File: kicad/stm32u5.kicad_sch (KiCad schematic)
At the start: 10 parts, among them SW5 BOOTSEL, U12 STM32U535CET6-modified

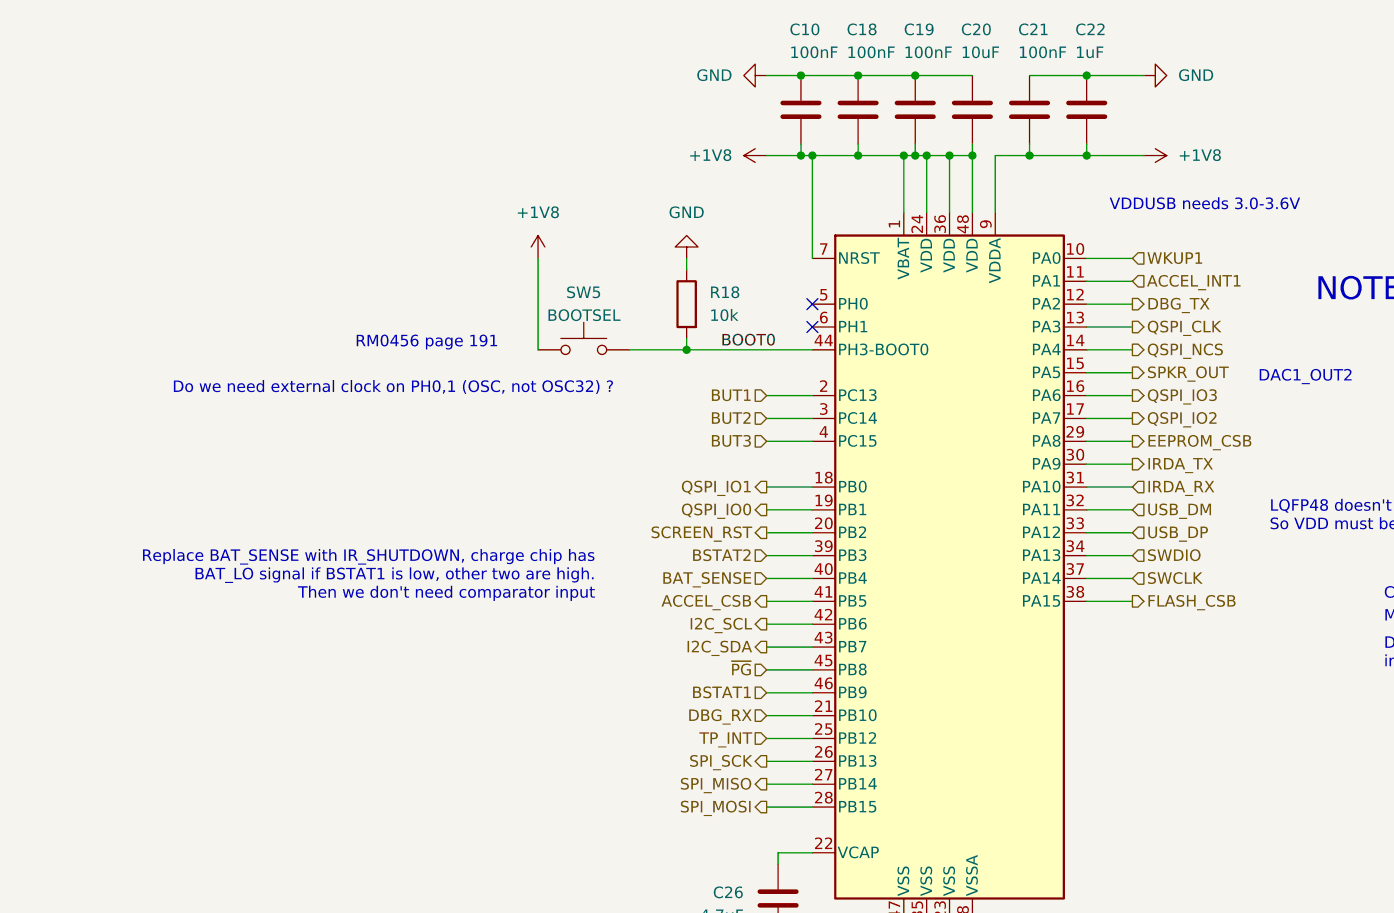
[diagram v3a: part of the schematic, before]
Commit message: hw: change to 3v3 LDO and remove unnecessary MCU pins
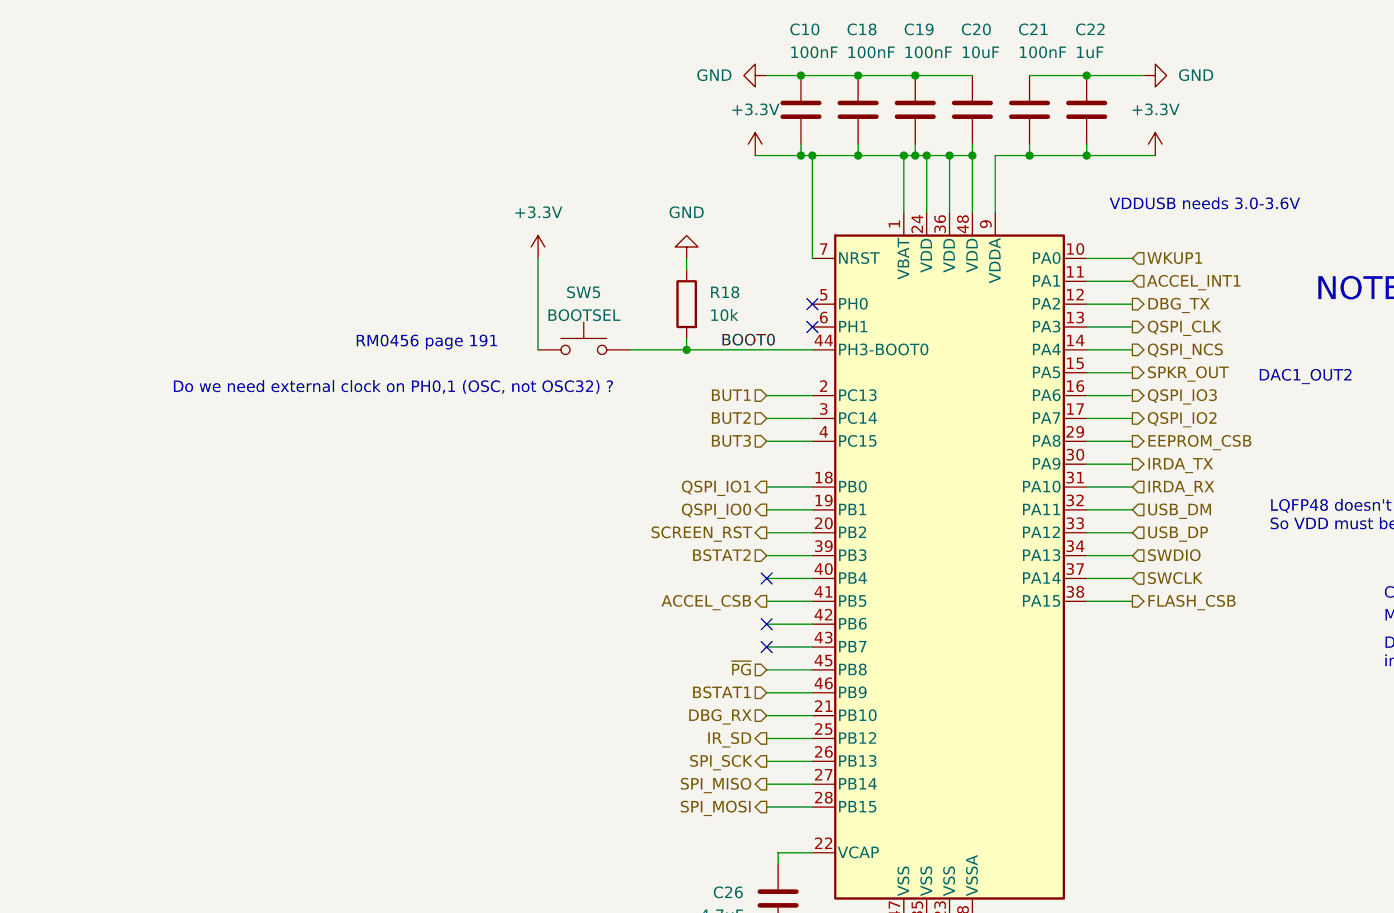
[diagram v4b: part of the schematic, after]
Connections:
- net +1V8 renamed +3.3V
- net BAT_SENSE: no longer names the net of U12.40 (PB4)
- net I2C_SCL: no longer names the net of U12.42 (PB6)
- net I2C_SDA: no longer names the net of U12.43 (PB7)
- net TP_INT renamed IR_SD
- no-connect marks 2 -> 5
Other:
- note removed: "Replace BAT_SENSE with IR_SHUTDOWN, charge chip has BAT_LO signal if BSTAT1 is low, other two are high. Then we don't need comparator input"
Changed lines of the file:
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@@
   (junction (at 110.49 33.02) (diameter 0) (color 0 0 0 0)
   )
+  (no_connect (at 95.25 85.09))
   (no_connect (at 100.33 52.07))
+  (no_connect (at 95.25 80.01))
+  (no_connect (at 95.25 87.63))
   (no_connect (at 100.33 49.53))
   (wire (pts (xy 115.57 33.02) (xy 118.11 33.02))
@@
     (stroke (width 0) (type default))
   )
+  (wire (pts (xy 130.81 33.02) (xy 138.43 33.02))
+    (stroke (width 0) (type default))
+  )
   (wire (pts (xy 130.81 64.77) (xy 135.89 64.77))
     (stroke (width 0) (type default))
@@
     (stroke (width 0) (type default))
   )
-  (wire (pts (xy 95.25 33.02) (xy 99.06 33.02))
+  (wire (pts (xy 93.98 33.02) (xy 99.06 33.02))
     (stroke (width 0) (type default))
   )
@@
     (stroke (width 0) (type default))
   )
+  (wire (pts (xy 95.25 97.79) (xy 100.33 97.79))
+    (stroke (width 0) (type default))
+  )
   (wire (pts (xy 130.81 82.55) (xy 135.89 82.55))
     (stroke (width 0) (type default))
@@
     (stroke (width 0) (type default))
   )
-  (wire (pts (xy 130.81 33.02) (xy 137.16 33.02))
-    (stroke (width 0) (type default))
-  )
   (wire (pts (xy 100.33 110.49) (xy 96.52 110.49))
     (stroke (width 0) (type default))
@@
   )
   (wire (pts (xy 110.49 119.38) (xy 96.52 119.38))
-    (stroke (width 0) (type default))
-  )
-  (wire (pts (xy 95.25 97.79) (xy 100.33 97.79))
     (stroke (width 0) (type default))
   )
@@
     (effects (font (size 1.27 1.27)) (justify left bottom))
   )
-  (text "Replace BAT_SENSE with IR_SHUTDOWN, charge chip has \nBAT_LO signal if BSTAT1 is low, other two are high.\nThen we don't need comparator input"
-    (at 76.2 82.55 0)
-    (effects (font (size 1.27 1.27)) (justify right bottom))
-  )
   (text "DAC1_OUT2" (at 149.86 58.42 0)
     (effects (font (size 1.27 1.27)) (justify left bottom))
@@
     (effects (font (size 1.27 1.27)) (justify right))
   )
-  (hierarchical_label "I2C_SDA" (shape output) (at 95.25 87.63 180) (fields_autoplaced)
-    (effects (font (size 1.27 1.27)) (justify right))
-  )
   (hierarchical_label "QSPI_IO0" (shape output) (at 95.25 72.39 180) (fields_autoplaced)
     (effects (font (size 1.27 1.27)) (justify right))
@@
     (effects (font (size 1.27 1.27)) (justify right))
   )
-  (hierarchical_label "TP_INT" (shape input) (at 95.25 97.79 180) (fields_autoplaced)
-    (effects (font (size 1.27 1.27)) (justify right))
-  )
   (hierarchical_label "BUT3" (shape input) (at 95.25 64.77 180) (fields_autoplaced)
     (effects (font (size 1.27 1.27)) (justify right))
@@
     (effects (font (size 1.27 1.27)) (justify left))
   )
-  (hierarchical_label "I2C_SCL" (shape output) (at 95.25 85.09 180) (fields_autoplaced)
-    (effects (font (size 1.27 1.27)) (justify right))
-  )
   (hierarchical_label "BSTAT2" (shape input) (at 95.25 77.47 180) (fields_autoplaced)
     (effects (font (size 1.27 1.27)) (justify right))
@@
     (effects (font (size 1.27 1.27)) (justify left))
   )
-  (hierarchical_label "BAT_SENSE" (shape input) (at 95.25 80.01 180) (fields_autoplaced)
+  (hierarchical_label "IR_SD" (shape output) (at 95.25 97.79 180) (fields_autoplaced)
     (effects (font (size 1.27 1.27)) (justify right))
   )
@@
     )
   )
+  (symbol (lib_id "power:+3.3V") (at 138.43 33.02 0) (unit 1)
+    (in_bom yes) (on_board yes) (dnp no) (fields_autoplaced)
+    (property "Reference" "#PWR04" (at 138.43 36.83 0)
+      (effects (font (size 1.27 1.27)) hide)
+    )
+    (property "Value" "+3.3V" (at 138.43 27.94 0)
+      (effects (font (size 1.27 1.27)))
+    )
+    (property "Footprint" "" (at 138.43 33.02 0)
+      (effects (font (size 1.27 1.27)) hide)
+    )
+    (property "Datasheet" "" (at 138.43 33.02 0)
+      (effects (font (size 1.27 1.27)) hide)
+    )
+    (pin "1")
+    (instances
+      (project "picowalker-32"
+        (path "/17fa99ff-0271-4e85-b8d9-a0357d961230/a4aaed07-2715-44e0-aa85-ccb151a6a10c"
+          (reference "#PWR04") (unit 1)
+        )
+      )
+    )
+  )
   (symbol (lib_id "Device:R") (at 86.36 49.53 0) (mirror y) (unit 1)
     (in_bom yes) (on_board yes) (dnp no) (fields_autoplaced)
@@
     )
   )
-  (symbol (lib_id "power:+1V8") (at 69.85 44.45 0) (unit 1)
-    (in_bom yes) (on_board yes) (dnp no) (fields_autoplaced)
-    (property "Reference" "#PWR07" (at 69.85 48.26 0)
-      (effects (font (size 1.27 1.27)) hide)
-    )
-    (property "Value" "+1V8" (at 69.85 39.37 0)
-      (effects (font (size 1.27 1.27)))
-    )
-    (property "Footprint" "" (at 69.85 44.45 0)
-      (effects (font (size 1.27 1.27)) hide)
-    )
-    (property "Datasheet" "" (at 69.85 44.45 0)
-      (effects (font (size 1.27 1.27)) hide)
-    )
-    (pin "1")
-    (instances
-      (project "picowalker-32"
-        (path "/17fa99ff-0271-4e85-b8d9-a0357d961230/a4aaed07-2715-44e0-aa85-ccb151a6a10c"
-          (reference "#PWR07") (unit 1)
-        )
-      )
-    )
-  )
   (symbol (lib_id "power:GND") (at 86.36 44.45 180) (unit 1)
     (in_bom yes) (on_board yes) (dnp no) (fields_autoplaced)
@@
         (path "/17fa99ff-0271-4e85-b8d9-a0357d961230/a4aaed07-2715-44e0-aa85-ccb151a6a10c"
           (reference "#PWR08") (unit 1)
-        )
-      )
-    )
-  )
-  (symbol (lib_id "power:+1V8") (at 95.25 33.02 90) (unit 1)
-    (in_bom yes) (on_board yes) (dnp no) (fields_autoplaced)
-    (property "Reference" "#PWR03" (at 99.06 33.02 0)
-      (effects (font (size 1.27 1.27)) hide)
-    )
-    (property "Value" "+1V8" (at 91.44 33.02 90)
-      (effects (font (size 1.27 1.27)) (justify left))
-    )
-    (property "Footprint" "" (at 95.25 33.02 0)
-      (effects (font (size 1.27 1.27)) hide)
-    )
-    (property "Datasheet" "" (at 95.25 33.02 0)
-      (effects (font (size 1.27 1.27)) hide)
-    )
-    (pin "1")
-    (instances
-      (project "picowalker-32"
-        (path "/17fa99ff-0271-4e85-b8d9-a0357d961230/a4aaed07-2715-44e0-aa85-ccb151a6a10c"
-          (reference "#PWR03") (unit 1)
         )
       )
@@
     )
   )
+  (symbol (lib_id "power:+3.3V") (at 69.85 44.45 0) (unit 1)
+    (in_bom yes) (on_board yes) (dnp no) (fields_autoplaced)
+    (property "Reference" "#PWR07" (at 69.85 48.26 0)
+      (effects (font (size 1.27 1.27)) hide)
+    )
+    (property "Value" "+3.3V" (at 69.85 39.37 0)
+      (effects (font (size 1.27 1.27)))
+    )
+    (property "Footprint" "" (at 69.85 44.45 0)
+      (effects (font (size 1.27 1.27)) hide)
+    )
+    (property "Datasheet" "" (at 69.85 44.45 0)
+      (effects (font (size 1.27 1.27)) hide)
+    )
+    (pin "1")
+    (instances
+      (project "picowalker-32"
+        (path "/17fa99ff-0271-4e85-b8d9-a0357d961230/a4aaed07-2715-44e0-aa85-ccb151a6a10c"
+          (reference "#PWR07") (unit 1)
+        )
+      )
+    )
+  )
   (symbol (lib_id "Device:C") (at 111.76 27.94 0) (unit 1)
     (in_bom yes) (on_board yes) (dnp no)
@@
         (path "/17fa99ff-0271-4e85-b8d9-a0357d961230/a4aaed07-2715-44e0-aa85-ccb151a6a10c"
           (reference "C19") (unit 1)
+        )
+      )
+    )
+  )
+  (symbol (lib_id "power:+3.3V") (at 93.98 33.02 0) (unit 1)
+    (in_bom yes) (on_board yes) (dnp no) (fields_autoplaced)
+    (property "Reference" "#PWR03" (at 93.98 36.83 0)
+      (effects (font (size 1.27 1.27)) hide)
+    )
+    (property "Value" "+3.3V" (at 93.98 27.94 0)
+      (effects (font (size 1.27 1.27)))
+    )
+    (property "Footprint" "" (at 93.98 33.02 0)
+      (effects (font (size 1.27 1.27)) hide)
+    )
+    (property "Datasheet" "" (at 93.98 33.02 0)
+      (effects (font (size 1.27 1.27)) hide)
+    )
+    (pin "1")
+    (instances
+      (project "picowalker-32"
+        (path "/17fa99ff-0271-4e85-b8d9-a0357d961230/a4aaed07-2715-44e0-aa85-ccb151a6a10c"
+          (reference "#PWR03") (unit 1)
         )
       )
@@
         )
       )
-    )
-  )
-  (symbol (lib_id "power:+1V8") (at 137.16 33.02 270) (unit 1)
-    (in_bom yes) (on_board yes) (dnp no) (fields_autoplaced)
-    (property "Reference" "#PWR04" (at 133.35 33.02 0)
-      (effects (font (size 1.27 1.27)) hide)
-    )
-    (property "Value" "+1V8" (at 140.97 33.02 90)
-      (effects (font (size 1.27 1.27)) (justify left))
-    )
-    (property "Footprint" "" (at 137.16 33.02 0)
-      (effects (font (size 1.27 1.27)) hide)
-    )
-    (property "Datasheet" "" (at 137.16 33.02 0)
-      (effects (font (size 1.27 1.27)) hide)
-    )
-    (pin "1")
-    (instances
-      (project "picowalker-32"
-        (path "/17fa99ff-0271-4e85-b8d9-a0357d961230/a4aaed07-2715-44e0-aa85-ccb151a6a10c"
-          (reference "#PWR04") (unit 1)
-        )
-      )

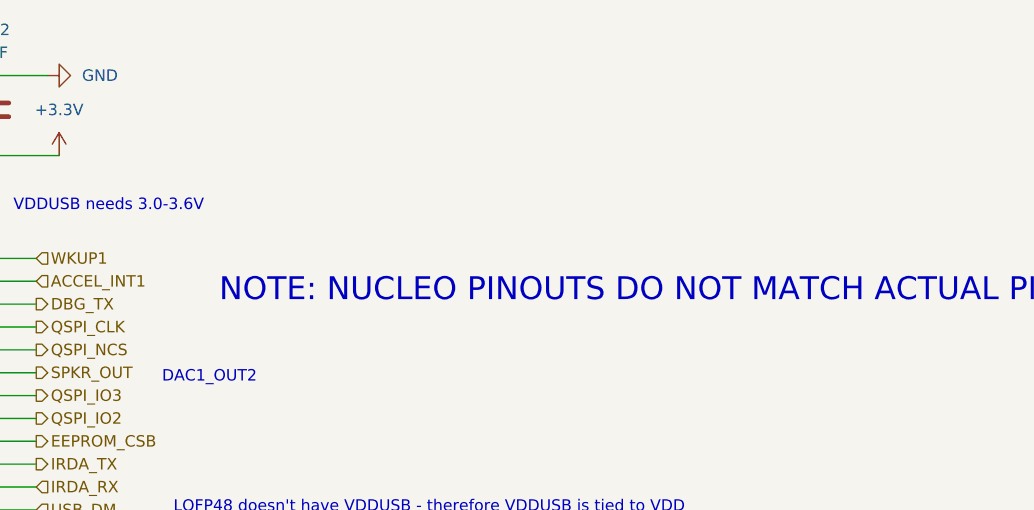
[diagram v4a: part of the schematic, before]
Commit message: hw: update power symbols, clean up some power circuitry
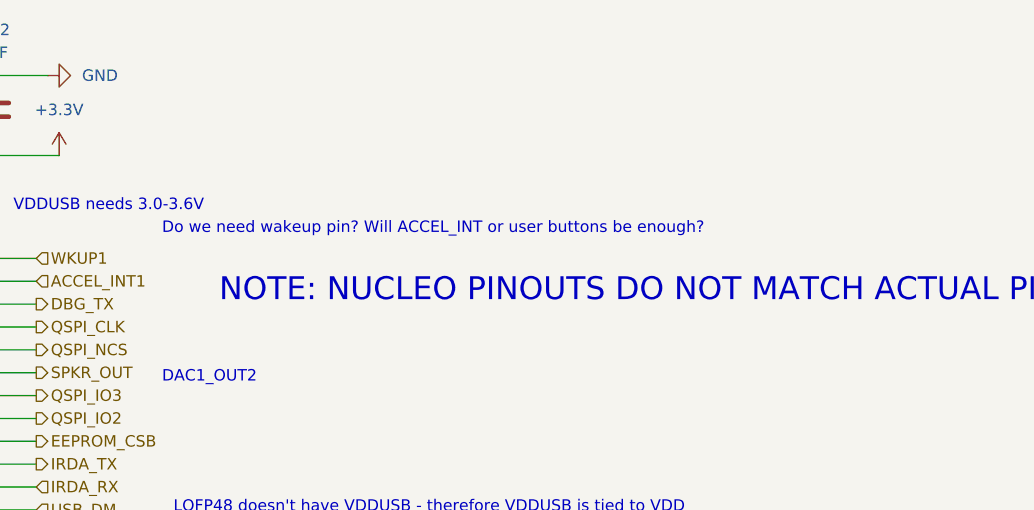
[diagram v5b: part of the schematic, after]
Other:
- note added: "Do we need wakeup pin? Will ACCEL_INT or user buttons be enough?"
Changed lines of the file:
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@@
+    (effects (font (size 1.27 1.27)) (justify left bottom))
+  )
+  (text "Do we need wakeup pin? Will ACCEL_INT or user buttons be enough?"
+    (at 149.86 41.91 0)
     (effects (font (size 1.27 1.27)) (justify left bottom))
   )
